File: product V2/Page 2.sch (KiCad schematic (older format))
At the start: 18 parts, among them Q1 Q_NMOS_GSD, Q2 Q_NMOS_GSD, Q3 Q_NMOS_GSD, SW1 1-1825027-1, U3 ESP32-WROOM-32D

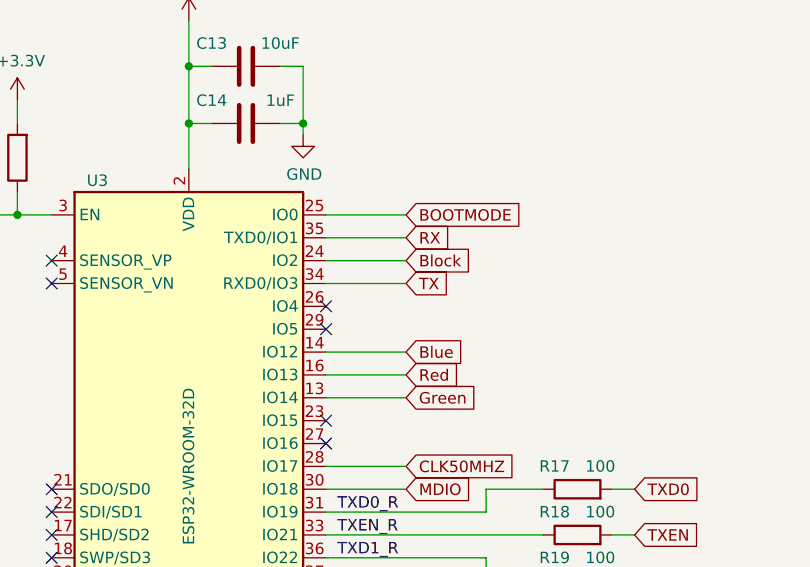
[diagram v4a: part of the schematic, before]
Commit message: Changed board outline and mounting to better fit inside enclosure
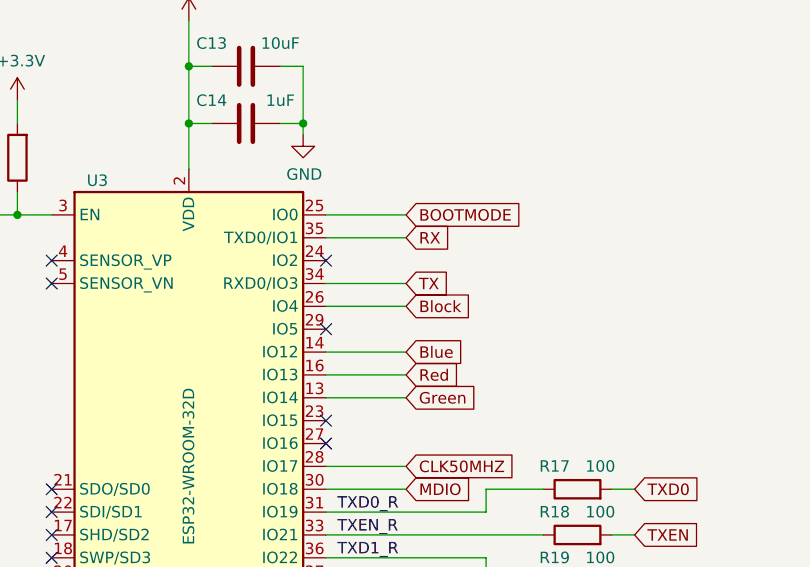
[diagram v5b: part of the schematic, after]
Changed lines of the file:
@@
 EESchema Schematic File Version 4
-LIBS:EsperDNS-cache
 EELAYER 30 0
 EELAYER END
@@
 Wire Wire Line
 	4600 2650 4950 2650
-NoConn ~ 4600 2950
+NoConn ~ 4600 2750
 NoConn ~ 4600 3050
 NoConn ~ 4600 3550
@@
 Text GLabel 4950 3350 2    50   Input ~ 0
 Green
-Wire Wire Line
-	4600 2750 4950 2750
-Text GLabel 4950 2750 2    50   Input ~ 0
+Text GLabel 4950 2950 2    50   Input ~ 0
 Block
+Wire Wire Line
+	4600 2950 4950 2950
 $EndSCHEMATC
